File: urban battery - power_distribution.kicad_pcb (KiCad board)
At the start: 2 copper layers, 19 parts, among them J1 FRONT_ACC_OUT, J2 12V_IN, J3 12VHC_OUT_EXTRA, J4 TEL_OUT, J5 REAR_ACC_OUT, J6 MTR_CTRL_OUT, J7 12VLC_OUT_EXTRA, J8 12VLC_OUT_EXTRA, J9 12VLC_OUT_EXTRA

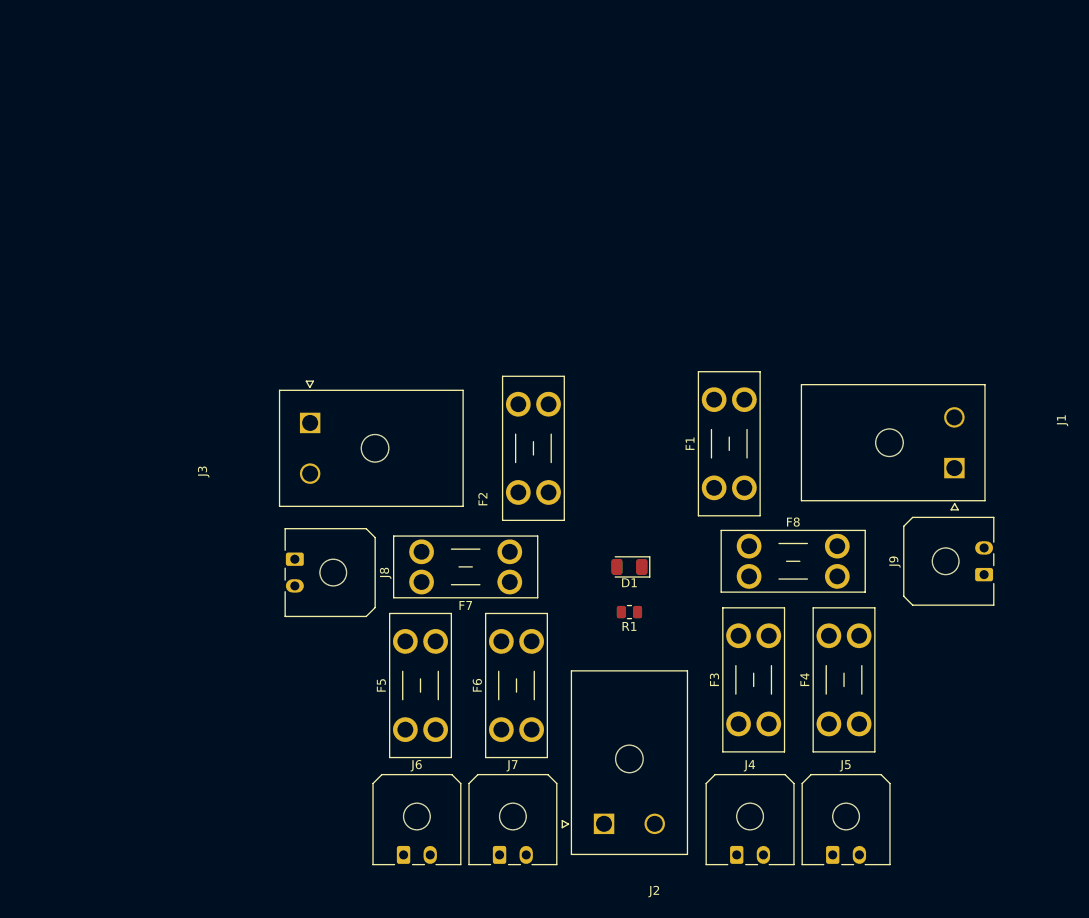
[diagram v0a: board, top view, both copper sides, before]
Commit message: updated layout, added logo
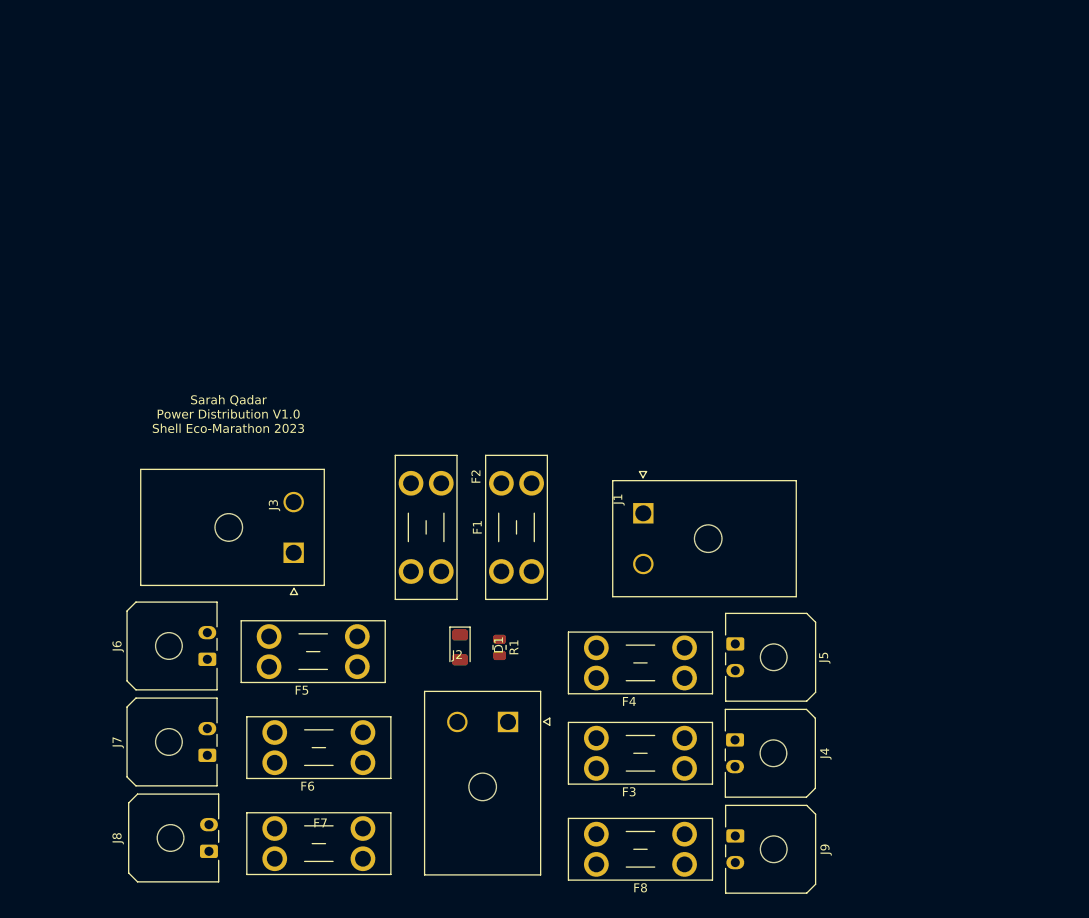
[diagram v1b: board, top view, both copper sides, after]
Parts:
- added G***: LOGO, LOGO, F.Cu at (146.1, 118.1)
- moved J9 40.6 mm to (151.6, 164.9), turned to -90 degrees
- moved F7 38.3 mm to (99.8, 164.0), turned to 0 degrees
- moved F8 36.5 mm to (145.9, 168.1), turned to 180 degrees
- moved J1 35.3 mm to (141.3, 128.6), turned to 90 degrees
- moved J7 34.7 mm to (92.2, 155.8), turned to 90 degrees
- moved J8 34.2 mm to (92.4, 166.6), turned to 90 degrees
- moved J6 31.2 mm to (92.2, 145.0), turned to 90 degrees
- moved J5 26.1 mm to (151.6, 143.3), turned to -90 degrees
- moved F1 25.7 mm to (125.3, 135.1)
- moved D1 21.1 mm to (120.7, 143.7), turned to -90 degrees
- moved F4 17.0 mm to (145.9, 147.1), turned to 180 degrees
- moved F6 16.0 mm to (109.7, 156.6), turned to 180 degrees
- moved J2 15.7 mm to (126.0, 152.1), turned to 0 degrees
- moved R1 15.1 mm to (125.1, 143.7), turned to -90 degrees
- moved J3 14.7 mm to (101.9, 133.0), turned to -90 degrees
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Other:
- board text added: "Sarah Qadar Power Distribution V1.0 Shell Eco-Marathon 2023"

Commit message: figuring out shape of board
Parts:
- moved F1 25.1 mm to (143.1, 117.5), turned to 0 degrees
- moved G*** 24.1 mm to (124.4, 128.8), turned to 45 degrees
- moved F2 16.2 mm to (102.9, 121.3), turned to 180 degrees
- moved J3 3.70 mm to (105.1, 134.9)
- moved J6 3.70 mm to (95.4, 146.9)
- moved J7 3.45 mm to (95.2, 157.5)
- moved J8 3.29 mm to (95.2, 168.3)
- moved F5 2.29 mm to (110.4, 147.8)
- moved F6 1.47 mm to (110.5, 157.9)
- moved F7 1.47 mm to (100.6, 165.3)
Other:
- board outline added: 75.6 x 61 mm
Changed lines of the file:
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@@
   (net 12 "Net-(D1-Pad2)")
   (footprint "Connector_Molex:Molex_Micro-Fit_3.0_43650-0200_1x02_P3.00mm_Horizontal" (layer "F.Cu")
-    (at 92.42 166.6 90)
+    (at 95.25 168.275 90)
     (descr "Molex Micro-Fit 3.0 Connector System, 43650-0200 (compatible alternatives: 43650-0201, 43650-0202), 2 Pins per row (https://www.molex.com/pdm_docs/sd/436500300_sd.pdf), generated with kicad-footprint-generator")
     (tags "connector Molex Micro-Fit_3.0 top entry")
@@
       (effects (font (size 1 1) (thickness 0.15)))
     )
-    (fp_text value "12VLC_OUT_EXTRA" (at 4.04 2.195 90) (layer "F.Fab")
+    (fp_text value "12VLC_OUT_EXTRA" (at 4.04 2.945 90) (layer "F.Fab")
       (effects (font (size 1 1) (thickness 0.15)))
     )
@@
   )
   (footprint "Connector_Molex:Molex_Micro-Fit_3.0_43650-0200_1x02_P3.00mm_Horizontal" (layer "F.Cu")
-    (at 92.235 145.01 90)
+    (at 95.41 146.915 90)
     (descr "Molex Micro-Fit 3.0 Connector System, 43650-0200 (compatible alternatives: 43650-0201, 43650-0202), 2 Pins per row (https://www.molex.com/pdm_docs/sd/436500300_sd.pdf), generated with kicad-footprint-generator")
     (tags "connector Molex Micro-Fit_3.0 top entry")
@@
       (effects (font (size 1 1) (thickness 0.15)))
     )
-    (fp_text value "MTR_CTRL_OUT" (at 1.5 3.22 90) (layer "F.Fab")
+    (fp_text value "MTR_CTRL_OUT" (at 1.5 3.97 90) (layer "F.Fab")
       (effects (font (size 1 1) (thickness 0.15)))
     )
@@
   )
   (footprint "LOGO" (layer "F.Cu")
-    (at 146.05 118.11)
+    (at 124.440185 128.818067 45)
     (attr board_only exclude_from_pos_files exclude_from_bom)
-    (fp_text reference "G***" (at 0 -1.27) (layer "F.Fab")
+    (fp_text reference "G***" (at 0 -1.27 45) (layer "F.Fab")
       (effects (font (size 1.524 1.524) (thickness 0.3)))
     )
-    (fp_text value "LOGO" (at 0.75 0) (layer "F.Fab") hide
+    (fp_text value "LOGO" (at 0.75 0 45) (layer "F.Fab") hide
       (effects (font (size 1.524 1.524) (thickness 0.3)))
     )
@@
   )
   (footprint "urban-power-dist-pcb-custom-footprints:MOLEX_2002411222" (layer "F.Cu")
-    (at 101.945 133.03 -90)
+    (at 105.12 134.935 -90)
     (property "Sheetfile" "File: urban battery - power_distribution.kicad_sch")
     (property "Sheetname" "")
     (attr through_hole)
-    (fp_text reference "J3" (at -5.395 2.25 90) (layer "F.SilkS")
-      (effects (font (size 1 1) (thickness 0.15)))
-    )
-    (fp_text value "12VHC_OUT_EXTRA" (at -2.22 -6.005 90) (layer "F.Fab")
+    (fp_text reference "J3" (at -5.395 1.5 90) (layer "F.SilkS")
+      (effects (font (size 1 1) (thickness 0.15)))
+    )
+    (fp_text value "12VHC_OUT_EXTRA" (at -2.22 -6.755 90) (layer "F.Fab")
       (effects (font (size 1 1) (thickness 0.15)))
     )
@@
       (effects (font (size 0.393701 0.393701) (thickness 0.15)))
     )
-    (fp_text user "PTH D1.8 +/- 0.05" (at -2.855 2.885 90) (layer "F.Fab")
+    (fp_text user "PTH D1.8 +/- 0.05" (at -2.855 2.135 90) (layer "F.Fab")
       (effects (font (size 0.393701 0.393701) (thickness 0.15)))
     )
@@
   )
   (footprint "Connector_Molex:Molex_Micro-Fit_3.0_43650-0200_1x02_P3.00mm_Horizontal" (layer "F.Cu")
-    (at 92.235 155.805 90)
+    (at 95.25 157.48 90)
     (descr "Molex Micro-Fit 3.0 Connector System, 43650-0200 (compatible alternatives: 43650-0201, 43650-0202), 2 Pins per row (https://www.molex.com/pdm_docs/sd/436500300_sd.pdf), generated with kicad-footprint-generator")
     (tags "connector Molex Micro-Fit_3.0 top entry")
@@
       (effects (font (size 1 1) (thickness 0.15)))
     )
-    (fp_text value "12VLC_OUT_EXTRA" (at 1.5 3.22 90) (layer "F.Fab")
+    (fp_text value "12VLC_OUT_EXTRA" (at 1.5 3.97 90) (layer "F.Fab")
       (effects (font (size 1 1) (thickness 0.15)))
     )
@@
   )
   (footprint "Fuse:Fuseholder_Blade_Mini_Keystone_3568" (layer "F.Cu")
-    (at 118.54 125.215 -90)
+    (at 102.87 121.285 180)
     (descr "fuse holder, car blade fuse mini, http://www.keyelco.com/product-pdf.cfm?p=306")
     (tags "car blade fuse mini")
@@
     (property "Sheetname" "")
     (attr through_hole)
-    (fp_text reference "F2" (at -0.755 -3.94 90) (layer "F.SilkS")
-      (effects (font (size 1 1) (thickness 0.15)))
-    )
-    (fp_text value "Fuse" (at 4.96 6.07 90) (layer "F.Fab")
-      (effects (font (size 1 1) (thickness 0.15)))
-    )
-    (fp_text user "${REFERENCE}" (at -0.755 0.43 90) (layer "F.Fab")
+    (fp_text reference "F2" (at -0.755 -3.94) (layer "F.SilkS")
+      (effects (font (size 1 1) (thickness 0.15)))
+    )
+    (fp_text value "Fuse" (at 4.96 5.32) (layer "F.Fab")
+      (effects (font (size 1 1) (thickness 0.15)))
+    )
+    (fp_text user "${REFERENCE}" (at -0.755 0.43) (layer "F.Fab")
       (effects (font (size 1 1) (thickness 0.15)))
     )
@@
     (fp_line (start -3.04 5.07) (end 12.96 5.07) (layer "F.Fab") (width 0.1))
     (fp_line (start 12.96 5.07) (end 12.96 -1.67) (layer "F.Fab") (width 0.1))
-    (pad "1" thru_hole circle (at 0 3.4 270) (size 2.78 2.78) (drill 1.78) (layers *.Cu *.Mask)
+    (pad "1" thru_hole circle (at 0 3.4 180) (size 2.78 2.78) (drill 1.78) (layers *.Cu *.Mask)
       (net 1 "+12V") (pintype "passive"))
-    (pad "1" thru_hole circle (at 0 0 270) (size 2.78 2.78) (drill 1.78) (layers *.Cu *.Mask)
+    (pad "1" thru_hole circle (at 0 0 180) (size 2.78 2.78) (drill 1.78) (layers *.Cu *.Mask)
       (net 1 "+12V") (pintype "passive"))
-    (pad "2" thru_hole circle (at 9.92 0 270) (size 2.78 2.78) (drill 1.78) (layers *.Cu *.Mask)
+    (pad "2" thru_hole circle (at 9.92 0 180) (size 2.78 2.78) (drill 1.78) (layers *.Cu *.Mask)
       (net 3 "Net-(F2-Pad2)") (pintype "passive"))
-    (pad "2" thru_hole circle (at 9.92 3.4 270) (size 2.78 2.78) (drill 1.78) (layers *.Cu *.Mask)
+    (pad "2" thru_hole circle (at 9.92 3.4 180) (size 2.78 2.78) (drill 1.78) (layers *.Cu *.Mask)
       (net 3 "Net-(F2-Pad2)") (pintype "passive"))
     (model "${KICAD6_3DMODEL_DIR}/Fuse.3dshapes/Fuseholder_Blade_Mini_Keystone_3568.wrl"
@@
   )
   (footprint "Fuse:Fuseholder_Blade_Mini_Keystone_3568" (layer "F.Cu")
-    (at 125.3 135.135 90)
+    (at 143.115 117.475)
     (descr "fuse holder, car blade fuse mini, http://www.keyelco.com/product-pdf.cfm?p=306")
     (tags "car blade fuse mini")
@@
     (property "Sheetname" "")
     (attr through_hole)
-    (fp_text reference "F1" (at 4.96 -2.67 90) (layer "F.SilkS")
-      (effects (font (size 1 1) (thickness 0.15)))
-    )
-    (fp_text value "Fuse" (at 4.96 6.07 90) (layer "F.Fab")
-      (effects (font (size 1 1) (thickness 0.15)))
-    )
-    (fp_text user "${REFERENCE}" (at 4.96 1.7 90) (layer "F.Fab")
+    (fp_text reference "F1" (at 4.96 -2.67) (layer "F.SilkS")
+      (effects (font (size 1 1) (thickness 0.15)))
+    )
+    (fp_text value "Fuse" (at 4.96 6.07) (layer "F.Fab")
+      (effects (font (size 1 1) (thickness 0.15)))
+    )
+    (fp_text user "${REFERENCE}" (at 4.96 1.7) (layer "F.Fab")
       (effects (font (size 1 1) (thickness 0.15)))
     )
@@
     (fp_line (start -3.04 -1.67) (end -3.04 5.07) (layer "F.Fab") (width 0.1))
     (fp_line (start 12.96 -1.67) (end -3.04 -1.67) (layer "F.Fab") (width 0.1))
-    (pad "1" thru_hole circle (at 0 3.4 90) (size 2.78 2.78) (drill 1.78) (layers *.Cu *.Mask)
+    (pad "1" thru_hole circle (at 0 3.4) (size 2.78 2.78) (drill 1.78) (layers *.Cu *.Mask)
       (net 1 "+12V") (pintype "passive"))
-    (pad "1" thru_hole circle (at 0 0 90) (size 2.78 2.78) (drill 1.78) (layers *.Cu *.Mask)
+    (pad "1" thru_hole circle (at 0 0) (size 2.78 2.78) (drill 1.78) (layers *.Cu *.Mask)
       (net 1 "+12V") (pintype "passive"))
-    (pad "2" thru_hole circle (at 9.92 3.4 90) (size 2.78 2.78) (drill 1.78) (layers *.Cu *.Mask)
+    (pad "2" thru_hole circle (at 9.92 3.4) (size 2.78 2.78) (drill 1.78) (layers *.Cu *.Mask)
       (net 2 "Net-(F1-Pad2)") (pintype "passive"))
-    (pad "2" thru_hole circle (at 9.92 0 90) (size 2.78 2.78) (drill 1.78) (layers *.Cu *.Mask)
+    (pad "2" thru_hole circle (at 9.92 0) (size 2.78 2.78) (drill 1.78) (layers *.Cu *.Mask)
       (net 2 "Net-(F1-Pad2)") (pintype "passive"))
     (model "${KICAD6_3DMODEL_DIR}/Fuse.3dshapes/Fuseholder_Blade_Mini_Keystone_3568.wrl"
@@
   )
   (footprint "Fuse:Fuseholder_Blade_Mini_Keystone_3568" (layer "F.Cu")
-    (at 109.1 145.845 180)
+    (at 110.37 147.75 180)
     (descr "fuse holder, car blade fuse mini, http://www.keyelco.com/product-pdf.cfm?p=306")
     (tags "car blade fuse mini")
@@
   )
   (footprint "Fuse:Fuseholder_Blade_Mini_Keystone_3568" (layer "F.Cu")
-    (at 109.735 156.64 180)
+    (at 110.485 157.91 180)
     (descr "fuse holder, car blade fuse mini, http://www.keyelco.com/product-pdf.cfm?p=306")
     (tags "car blade fuse mini")
@@
   )
   (footprint "Fuse:Fuseholder_Blade_Mini_Keystone_3568" (layer "F.Cu")
-    (at 99.815 164.035)
+    (at 100.565 165.305)
     (descr "fuse holder, car blade fuse mini, http://www.keyelco.com/product-pdf.cfm?p=306")
     (tags "car blade fuse mini")
@@
     )
   )
-  (gr_text "Sarah Qadar\nPower Distribution V1.0\nShell Eco-Marathon 2023" (at 94.615 117.475) (layer "F.SilkS")
+  (gr_poly
+    (pts
+      (xy 160.660169 111.125042)
+      (xy 161.29 171.45)
+      (xy 85.725 172.085)
+      (xy 85.725006 111.125)
+    ) (layer "Edge.Cuts") (width 0.1) (fill none))
+  (gr_text "Sarah Qadar    Power Distribution V1.0    Shell Eco-Marathon 2023" (at 124.46 113.03) (layer "F.SilkS")
     (effects (font (size 1 1) (thickness 0.15)))
   )

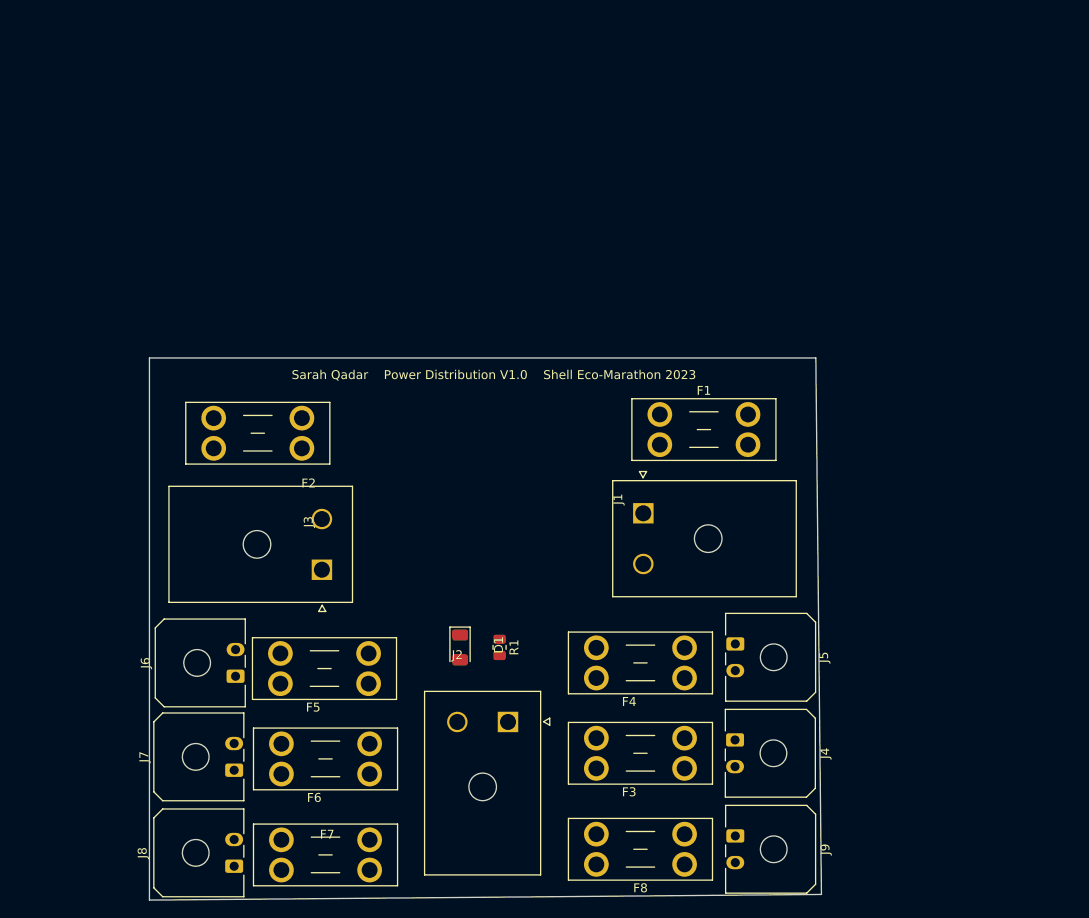
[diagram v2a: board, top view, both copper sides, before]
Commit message: completed moat of layout including pcb shape, fill zones, traces, logo, name and component arrangement
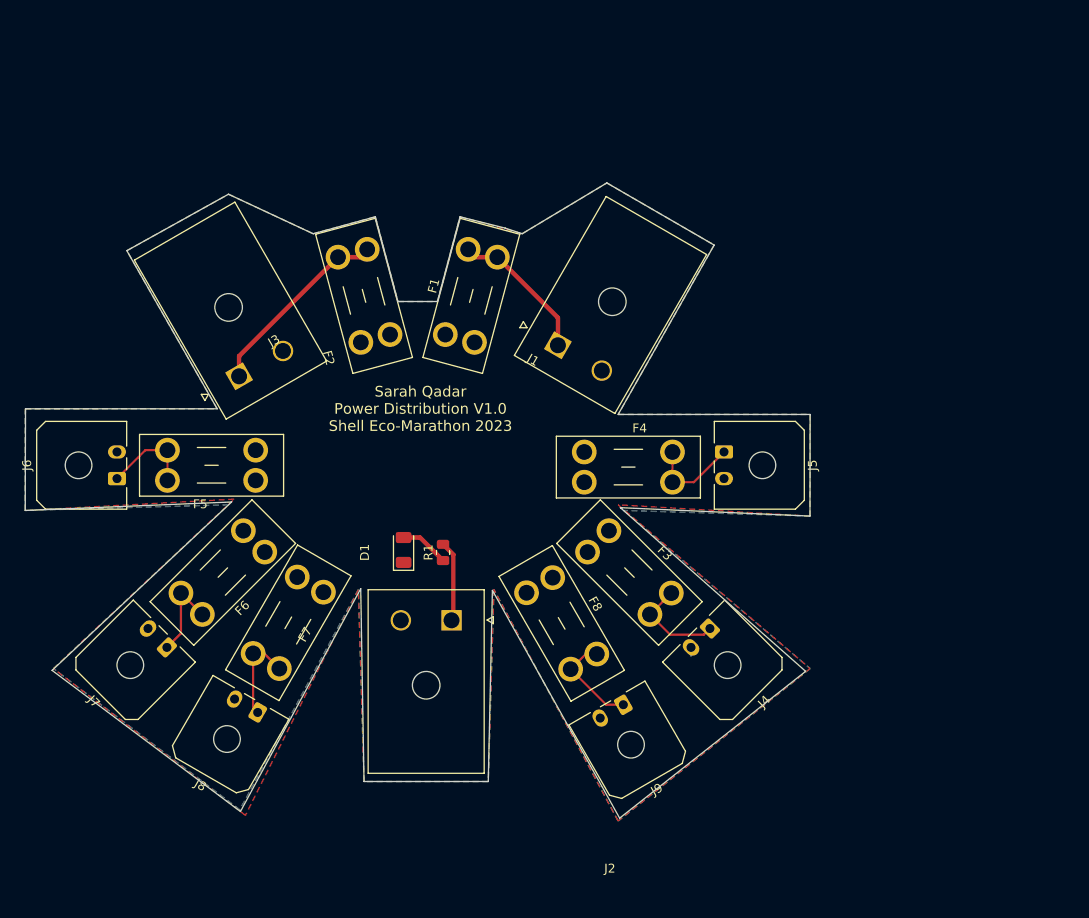
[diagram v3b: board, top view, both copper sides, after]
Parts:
- moved F8 35.5 mm to (131.1, 135.8), turned to -60 degrees
- moved F7 28.2 mm to (105.3, 137.5), turned to -120 degrees
- moved F3 28.0 mm to (137.4, 130.5), turned to -45 degrees
- moved F4 27.8 mm to (134.6, 121.7), turned to 0 degrees
- moved F6 27.6 mm to (98.7, 132.9), turned to -135 degrees
- moved F5 26.2 mm to (97.7, 124.9)
- moved J6 25.9 mm to (82.1, 124.7)
- moved F1 25.7 mm to (119.0, 108.5), turned to 75 degrees
- moved J3 23.7 mm to (95.8, 113.2), turned to -150 degrees
- moved J5 21.6 mm to (150.3, 121.7)
- moved J1 21.2 mm to (131.7, 109.7), turned to 150 degrees
- moved J9 19.4 mm to (139.0, 150.1), turned to -150 degrees
- moved J8 17.5 mm to (97.9, 151.0), turned to 150 degrees
- moved J7 15.7 mm to (87.7, 143.7), turned to 135 degrees
- moved F2 13.6 mm to (109.5, 109.4), turned to 105 degrees
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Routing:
- net Net-(F2-Pad2): track 0.00 -> 21.7 mm
- net Net-(F1-Pad2): track 0.00 -> 16.4 mm
- net Net-(F3-Pad2): track 0.00 -> 11.4 mm
- net Net-(F8-Pad2): track 0.00 -> 11.2 mm
- net Net-(F4-Pad2): track 0.00 -> 10.6 mm
- net Net-(F7-Pad2): track 0.00 -> 10.5 mm
- net Net-(F5-Pad2): track 0.00 -> 10.4 mm
- net Net-(F6-Pad2): track 0.00 -> 10.2 mm
- net Net-(J2-Pad1): track 0.00 -> 9.10 mm
- net Net-(D1-Pad2): track 0.00 -> 5.52 mm
- net GND: track 0.00 -> 0.93 mm
- added copper zone on F.Cu, net +12V
- added copper zone on B.Cu, net GND
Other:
- board size 75.6 x 61 mm -> 88.3 x 71.4 mm
